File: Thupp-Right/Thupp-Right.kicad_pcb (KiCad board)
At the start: 2 copper layers, 42 parts

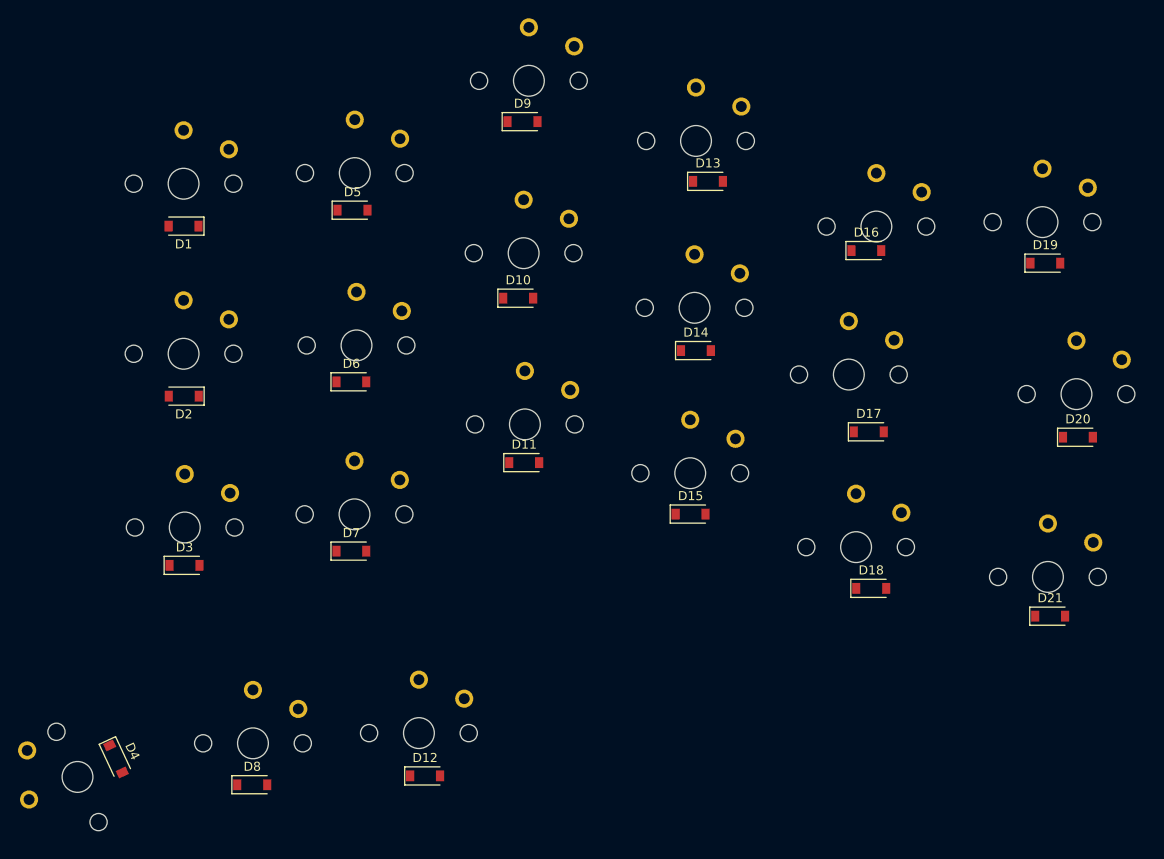
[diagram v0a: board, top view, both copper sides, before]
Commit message: footprints placed
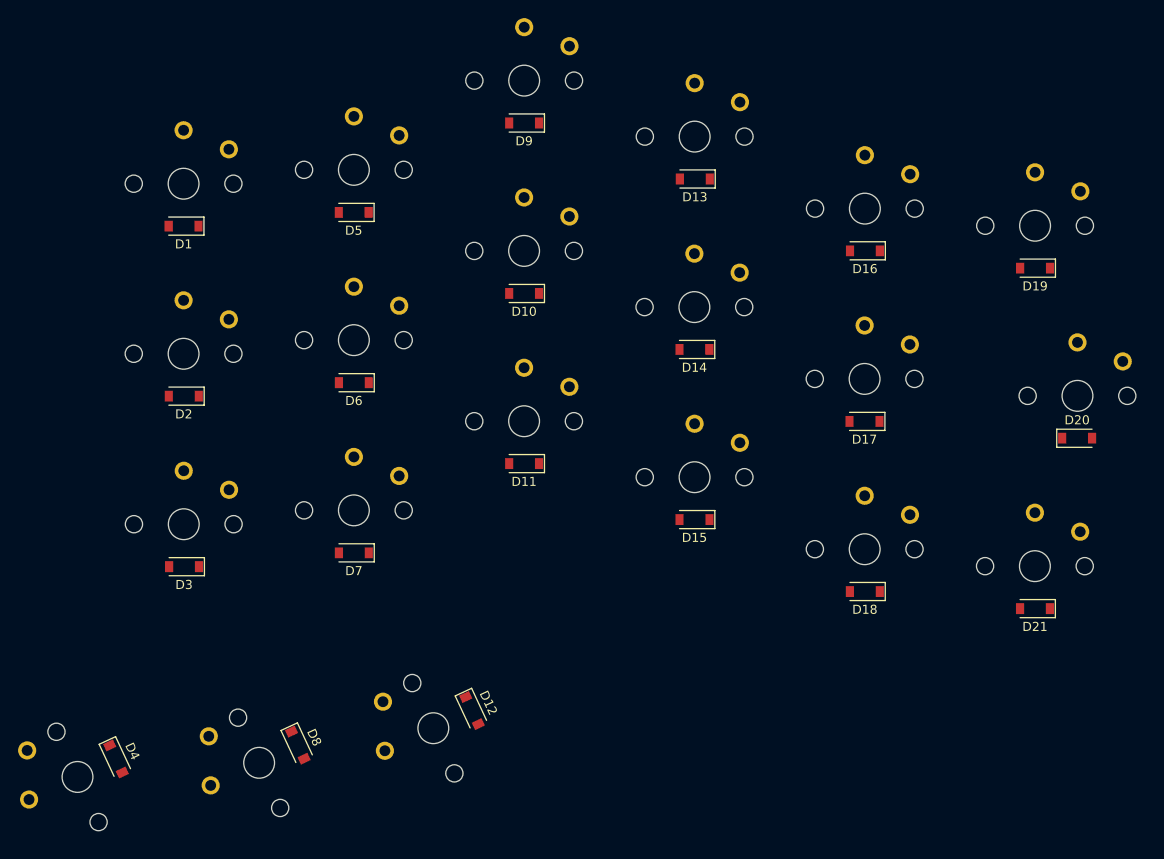
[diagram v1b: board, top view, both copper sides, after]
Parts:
- moved D12 8.88 mm to (79.7, 98.8), turned to 295 degrees
- moved D8 6.66 mm to (60.5, 102.6), turned to 295 degrees
- moved MX16 2.35 mm to (123.1, 43.4)
- moved MX8 2.25 mm to (56.2, 104.5), turned to 115 degrees
- moved MX21 1.87 mm to (141.9, 82.8)
- moved D21 1.86 mm to (141.9, 87.5), turned to 180 degrees
- moved MX17 1.80 mm to (123.1, 62.1)
- moved MX12 1.68 mm to (75.5, 100.7), turned to 115 degrees
- moved D13 1.47 mm to (104.3, 40.1), turned to 180 degrees
- moved D19 1.26 mm to (141.9, 49.9), turned to 180 degrees
- moved D17 1.24 mm to (123.0, 66.8), turned to 180 degrees
- moved MX18 0.98 mm to (123.1, 81.0)
- moved MX19 0.91 mm to (141.9, 45.2)
- moved D10 0.83 mm to (85.5, 52.7), turned to 180 degrees
- moved D18 0.78 mm to (123.1, 85.6), turned to 180 degrees
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
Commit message: aligned footprints relative to plate
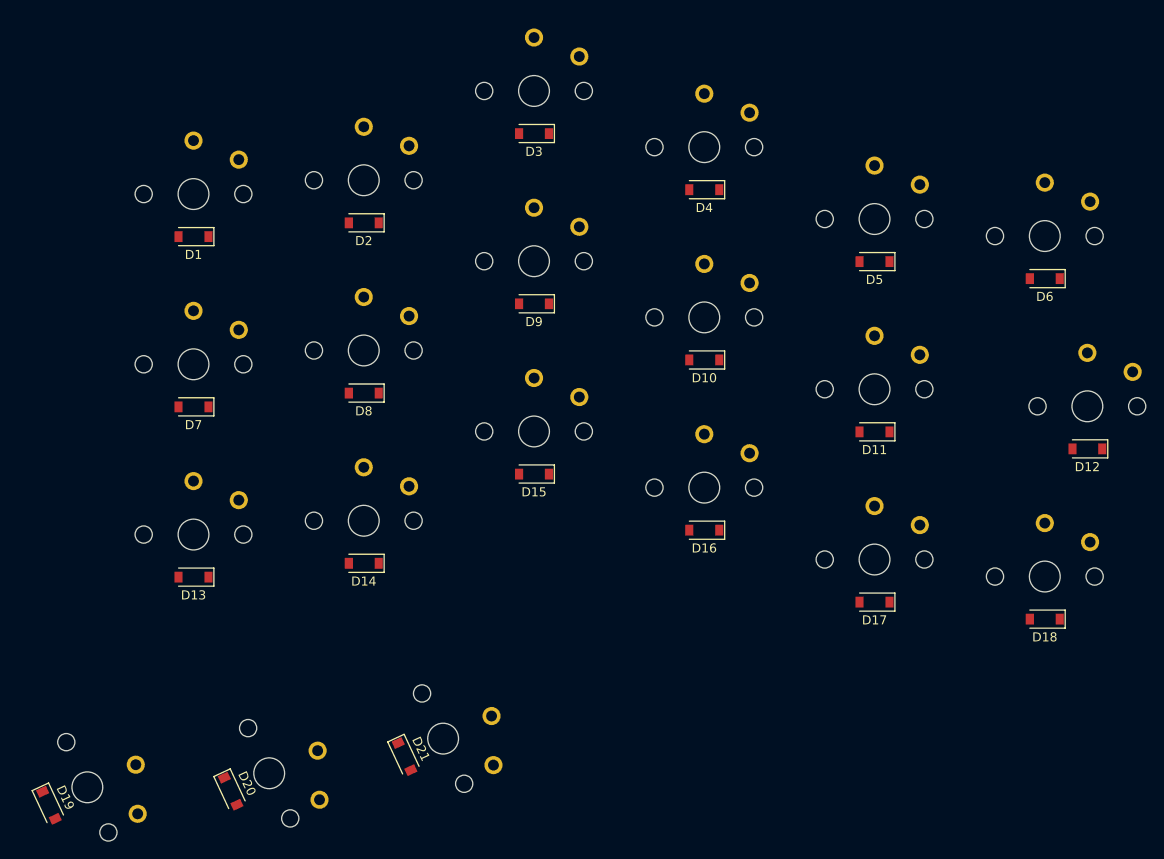
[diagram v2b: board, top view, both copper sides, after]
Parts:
- MX19: footprint Kailh_Choc:KailhChoc-1U -> Kailh_Choc:KailhChoc-2U
- MX21: footprint Kailh_Choc:KailhChoc-1U -> Kailh_Choc:KailhChoc-1.5U
- MX4: footprint Kailh_Choc:KailhChoc-2U -> Kailh_Choc:KailhChoc-1U
- MX8: footprint Kailh_Choc:KailhChoc-1.5U -> Kailh_Choc:KailhChoc-1U
- moved D19 124.0 mm to (33.0, 109.2), turned to 295 degrees
- moved MX19 121.6 mm to (37.3, 107.2), turned to 295 degrees
- moved D20 101.2 mm to (53.1, 107.7), turned to 295 degrees
- moved MX20 98.5 mm to (57.3, 105.7), turned to 295 degrees
- moved MX4 98.1 mm to (105.4, 36.6), turned to 0 degrees
- moved D4 90.4 mm to (105.4, 41.3), turned to 180 degrees
- moved MX12 80.5 mm to (147.7, 65.2), turned to 0 degrees
- moved D6 77.1 mm to (143.0, 51.1)
- moved MX6 77.1 mm to (143.0, 46.4)
- moved D12 73.8 mm to (147.7, 69.9), turned to 180 degrees
- moved D21 71.5 mm to (72.3, 103.8), turned to 295 degrees
- moved D13 70.7 mm to (49.0, 84.0)
- moved MX13 70.6 mm to (49.0, 79.3)
- moved MX21 68.0 mm to (76.5, 101.9), turned to 295 degrees
- moved MX3 61.5 mm to (86.6, 30.4)
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
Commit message: adding col assn to nice!nano
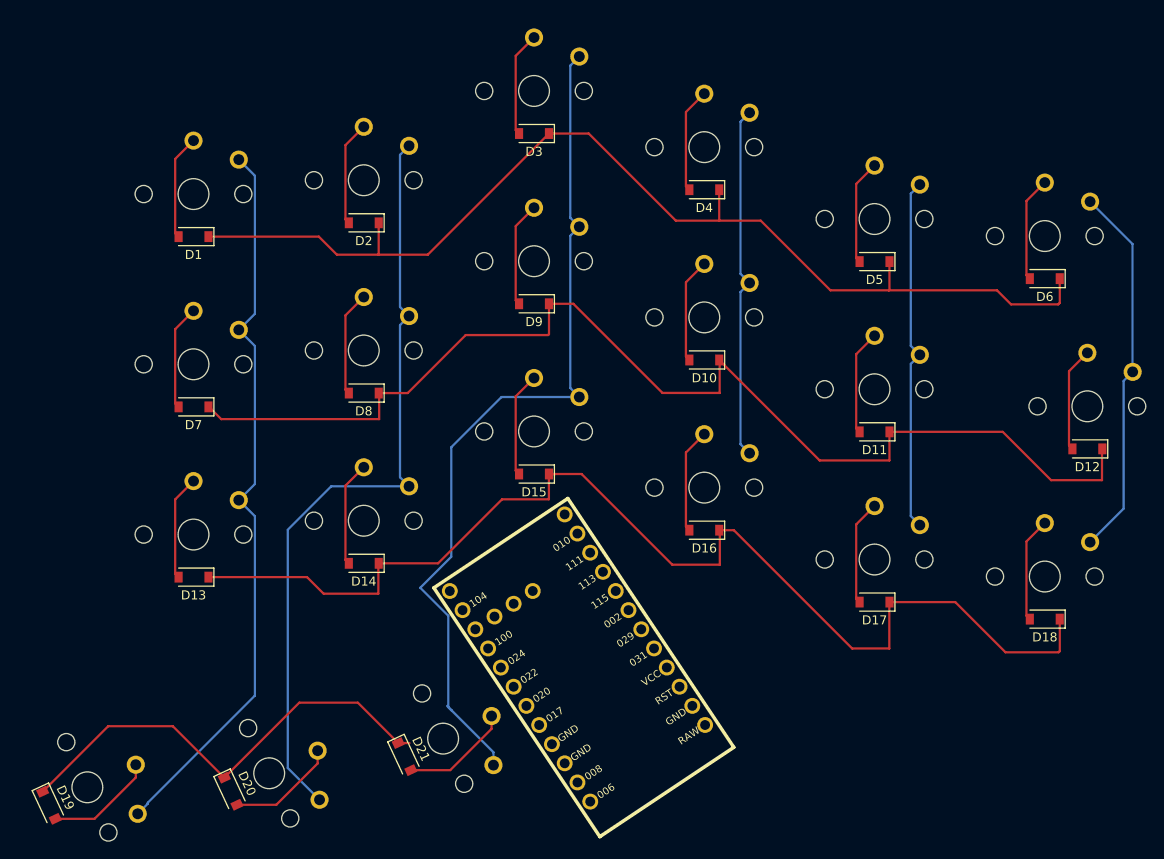
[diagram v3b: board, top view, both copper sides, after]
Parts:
- added U1: nice_nano, nice-nano-kicad:nice_nano, B.Cu at (91.4, 93.0)
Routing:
- net ROW1: track 0.00 -> 129.4 mm
- net ROW2: track 0.00 -> 128.2 mm
- net ROW0: track 0.00 -> 121.1 mm
- net COL2: track 0.00 -> 96.3 mm
- net COL1: track 0.00 -> 85.9 mm
- net COL0: track 0.00 -> 81.3 mm
- net ROW3: track 0.00 -> 51.1 mm
- net COL5: track 0.00 -> 41.5 mm
- net COL3: track 0.00 -> 39.2 mm
- net COL4: track 0.00 -> 39.2 mm
- net Net-(D21-Pad2): track 0.00 -> 12.2 mm
- net Net-(D20-Pad2): track 0.00 -> 12.2 mm
- net Net-(D19-Pad2): track 0.00 -> 12.2 mm
- net Net-(D9-Pad2): track 0.00 -> 11.6 mm
- net Net-(D18-Pad2): track 0.00 -> 11.6 mm
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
